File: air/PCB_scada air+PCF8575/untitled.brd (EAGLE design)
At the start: 170.5 x 95 mm, 122 parts, among them J1 C-GRID-03-70543, J10 C-GRID-03-70543, J11 C-GRID-03-70543, J12 C-GRID-03-70543, J13 C-GRID-03-70543, J14 C-GRID-03-70543, J15 C-GRID-03-70543, J16 C-GRID-03-70543, J17 C-GRID-03-70543, J18 C-GRID-03-70543, J19 C-GRID-03-70543, J2 C-GRID-03-70543, J20 C-GRID-03-70543, J21 C-GRID-03-70543, J3 C-GRID-03-70543, J4 C-GRID-03-70543, J5 C-GRID-03-70543, J6 C-GRID-03-70543, J7 C-GRID-03-70543, J8 C-GRID-03-70543, J9 C-GRID-03-70543, K1 351, Q1 MMBT2222, Q10 MMBT2222, Q11 MMBT2222, Q12 MMBT2222, Q13 MMBT2222, Q14 MMBT2222, Q15 MMBT2222, Q16 MMBT2222, Q17 MMBT2222, Q18 MMBT2222, Q19 MMBT2222, Q2 MMBT2222, Q20 MMBT2222, Q21 MMBT2222, Q22 S9013, Q3 MMBT2222, Q4 MMBT2222, Q5 MMBT2222, Q6 MMBT2222, Q7 MMBT2222, Q8 MMBT2222, Q9 MMBT2222, U1 ESP32-DEVKITC-32D, U2 PCF8575PW, U3 PCF8575PW, U4 PC817X2NIP0F, X1 C-GRID-02-70543, X2 C-GRID-02-70543, X3 MSTBA2, X4 C-GRID-03-70543, X5 C-GRID-02-70543, X6 C-GRID-02-70543, X7 MSTBA2, X8 MSTBA4, X9 MSTBA2

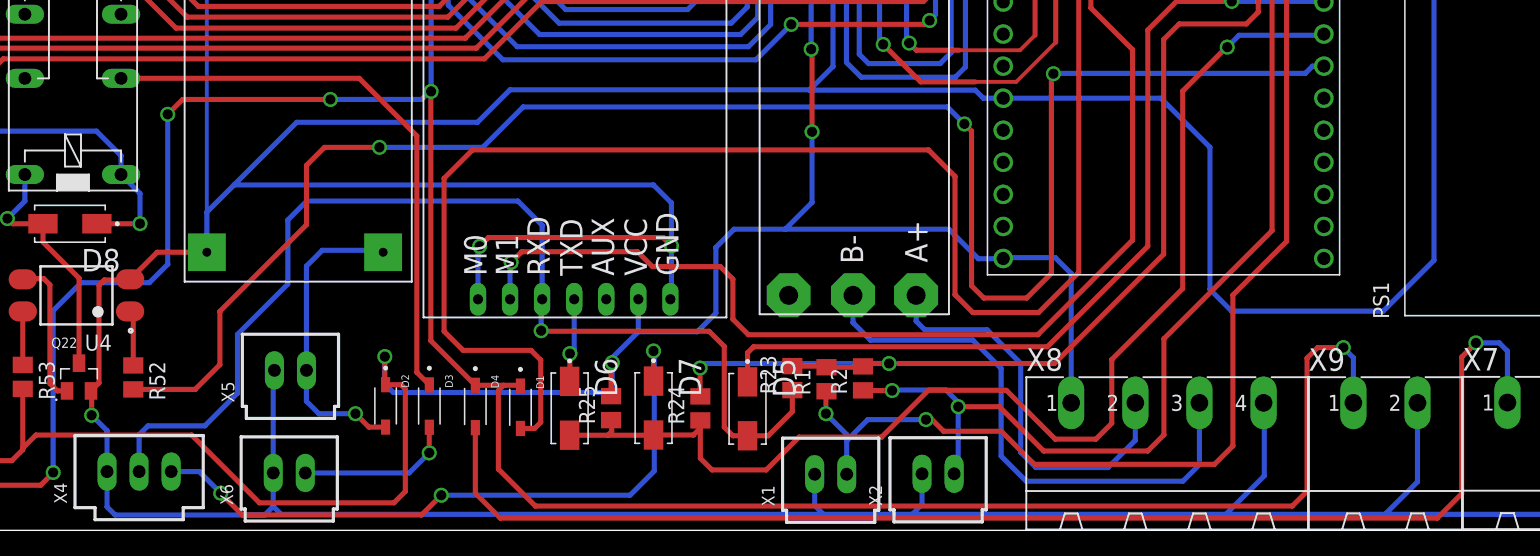
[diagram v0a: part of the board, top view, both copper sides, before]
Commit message: revisi dioda schotky
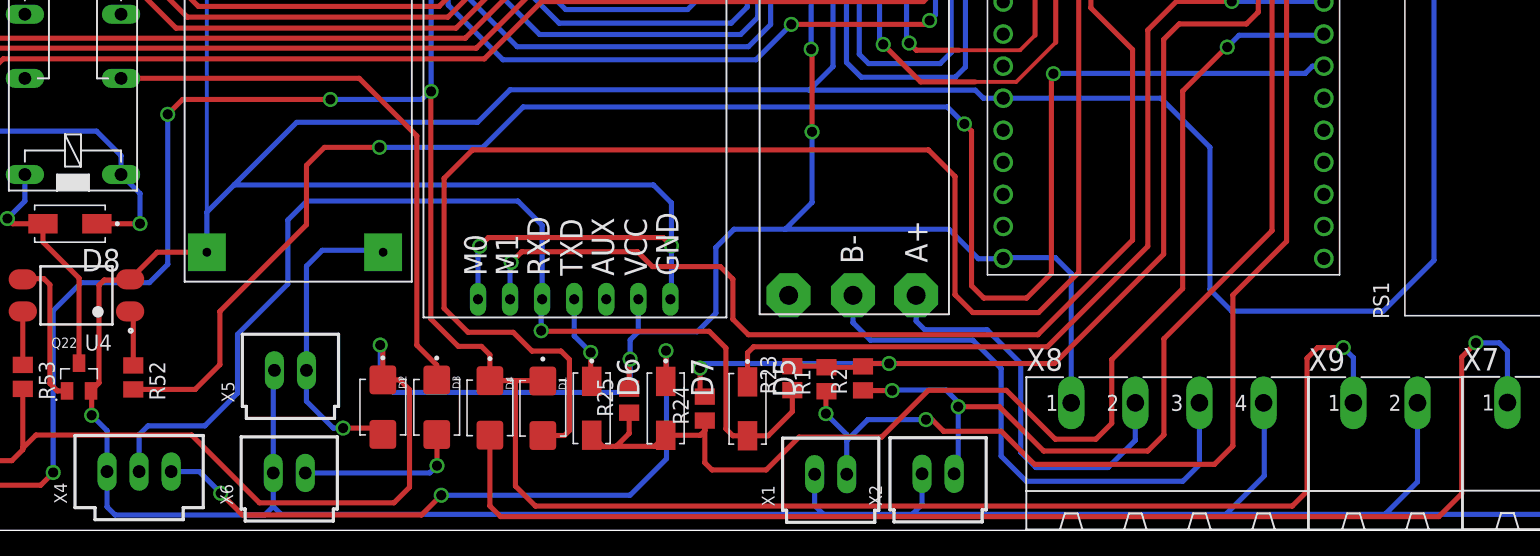
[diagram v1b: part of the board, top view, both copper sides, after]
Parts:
- D1, D2, D3, D4: value 1N5819HW-7 -> SS24; device 1N5819HW-7:SOD3715X145N -> SS24:DIOM5336X265N
- moved D1 1.77 mm to (67.2, 19.7)
- moved D6 1.75 mm to (71.1, 19.7)
- moved R25 1.55 mm to (74.1, 20.3)
- moved D4 1.16 mm to (63.0, 19.7)
- moved D7 0.97 mm to (77.0, 19.7)
- moved D3 0.59 mm to (58.8, 19.8)
- moved R24 0.36 mm to (80.1, 19.6)
- moved D2 0.24 mm to (54.5, 19.8)
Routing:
- net VCC: track 669.2 -> 671.8 mm
- net 12V++: track 232.4 -> 234.7 mm
- net 12V+: track 735.0 -> 736.5 mm
- net N$22: track 104.2 -> 103.0 mm
- net N$3: track 12.5 -> 13.6 mm
- net TX_LORA: track 95.0 -> 96.0 mm

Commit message: revisi scada air
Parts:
- added JP1, JP2: (no value), adafruit:1X03-CLEANBIG
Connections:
- new net GND1: JP1.1, JP1.2, JP1.3, JP2.1, JP2.2, JP2.3
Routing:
- net VCC: track 671.8 -> 668.1 mm
- net 12V+: track 736.5 -> 733.4 mm
- net TX_LORA: track 96.0 -> 98.5 mm
- net CYBLE1: track 104.5 -> 105.7 mm
- net CYBLE2: track 95.1 -> 96.3 mm
- net GND: track 920.6 -> 921.3 mm
- net 3V3: track 145.3 -> 144.6 mm
- added copper zone on layer 1, net GND1
- added copper zone on layer 16, net GND1
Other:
- board text added: "12V+"
- board text added: "12V-"
- board text added: "5V+"
- board text added: "5V-"
- board text added: "A+"
- board text added: "B-"
- board text added: "BATTERY"
- board text added: "CYBLE"
- board text added: "CYBLE1"
- board text added: "GND"
- board text added: "IN+"
- board text added: "IN1"
- board text added: "IN10"
- board text added: "IN11"
- board text added: "IN12"
- board text added: "IN13"
- board text added: "IN14"
- board text added: "IN15"
- board text added: "IN16"
- board text added: "IN17"
- board text added: "IN18"
- board text added: "IN19"
- board text added: "IN2"
- board text added: "IN20"
- board text added: "IN21"
- board text added: "IN3"
- board text added: "IN4"
- board text added: "IN5"
- board text added: "IN6"
- board text added: "IN7"
- board text added: "IN8"
- board text added: "IN9"
- board text added: "L"
- board text added: "N"
- board text added: "RX"
- board text added: "TX"
